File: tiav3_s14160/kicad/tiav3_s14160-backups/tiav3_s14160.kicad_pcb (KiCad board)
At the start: 4 copper layers, 25.3 x 25.3 mm, 24 parts, among them J1 SSQ-103-01-G-D, J2 Conn_Coaxial, J3 Snibbor Inc LOGO, J4 Bennett close LOGO, U1 OPA847IDBVT

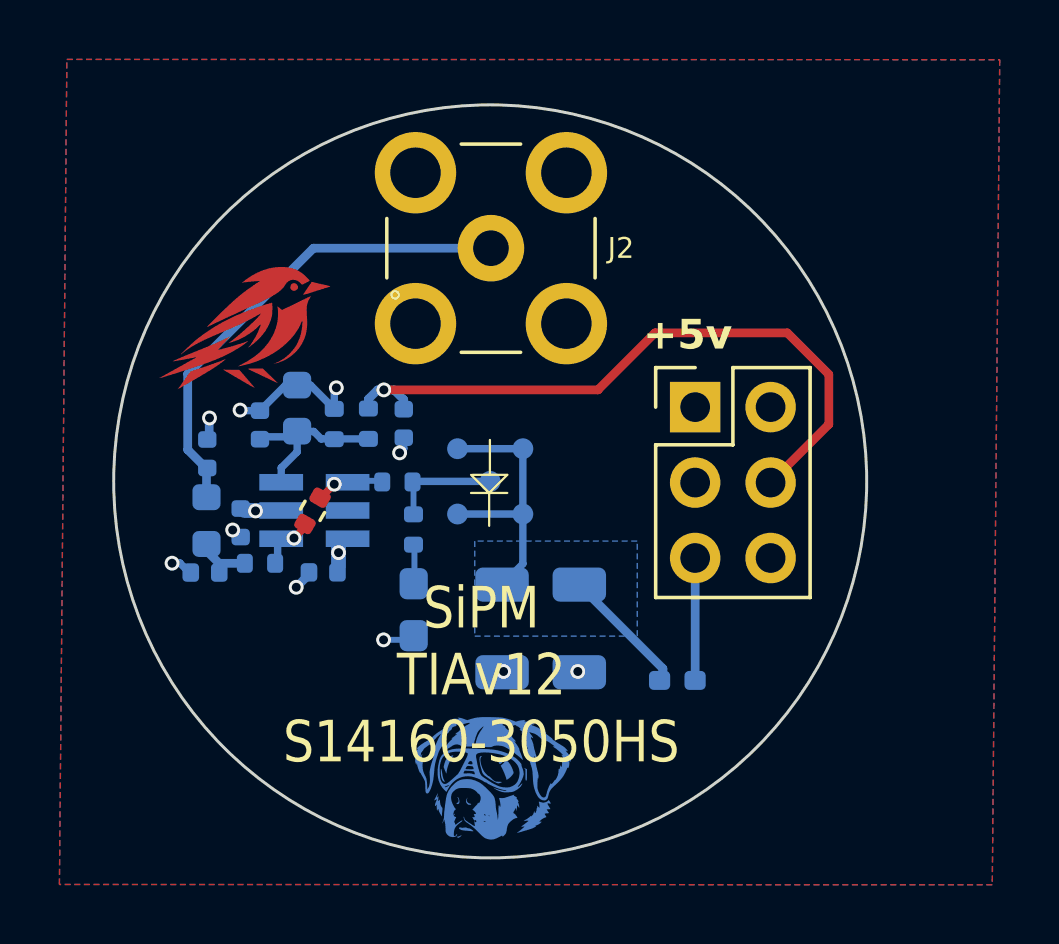
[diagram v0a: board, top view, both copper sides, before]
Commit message: updating s14160-3050HS footprint
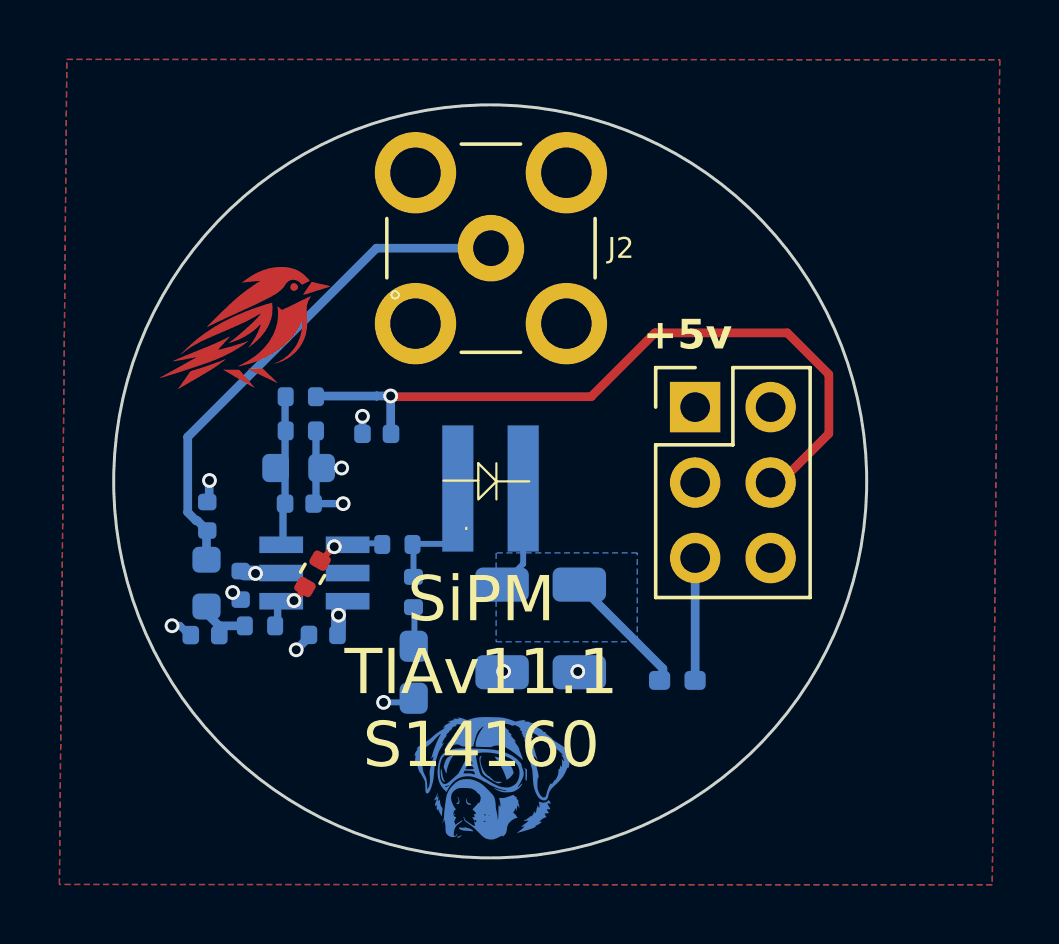
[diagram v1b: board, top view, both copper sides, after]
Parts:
- D2: value S14160-3050HS -> S14160-30; footprint footprints:S14160-3050HS -> footprints:S14160-30
- moved C7 2.96 mm to (193.6, 100.8), turned to 0 degrees
- moved R7 2.45 mm to (193.6, 97.2), turned to 0 degrees
- moved R2 2.12 mm to (194.0, 103.1)
- moved C2 2.11 mm to (190.4, 105.2)
- moved C3 2.11 mm to (190.5, 101.2)
- moved C5 2.11 mm to (194.4, 105.2)
- moved C9 2.11 mm to (191.6, 103.5)
- moved L1 2.11 mm to (197.4, 106.4)
- moved L2 2.11 mm to (190.4, 103.4)
- moved R1 2.11 mm to (192.2, 104.9)
- moved R23 2.11 mm to (196.9, 102.1)
- moved R5 2.10 mm to (197.4, 103.7)
- moved U1 2.10 mm to (194.1, 103.1)
- moved C8 2.02 mm to (193.6, 99.5), turned to 0 degrees
- moved R3 1.15 mm to (193.6, 98.3), turned to 180 degrees
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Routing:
- net /VBiasFilt: track 13.6 -> 7.92 mm
- net LINE: track 22.9 -> 24.7 mm
- net Net-(D2-A): track 3.53 -> 2.27 mm
- net Net-(U1-+): track 5.69 -> 4.92 mm
- net Net-(J2-In): track 16.5 -> 17.3 mm
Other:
- board text added: "SiPM TIAv11.1 S14160"
- board text removed: "SiPM TIAv12 S14160-3050HS"
